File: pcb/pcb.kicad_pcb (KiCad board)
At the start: 2 copper layers, 201 x 76 mm, 21 parts, among them J1 encoder, J2 programmer, J4 usb-ttl, SW1 reset, SW2 play/pause, SW3 prev track, SW4 next track, U1 ATmega32-16P

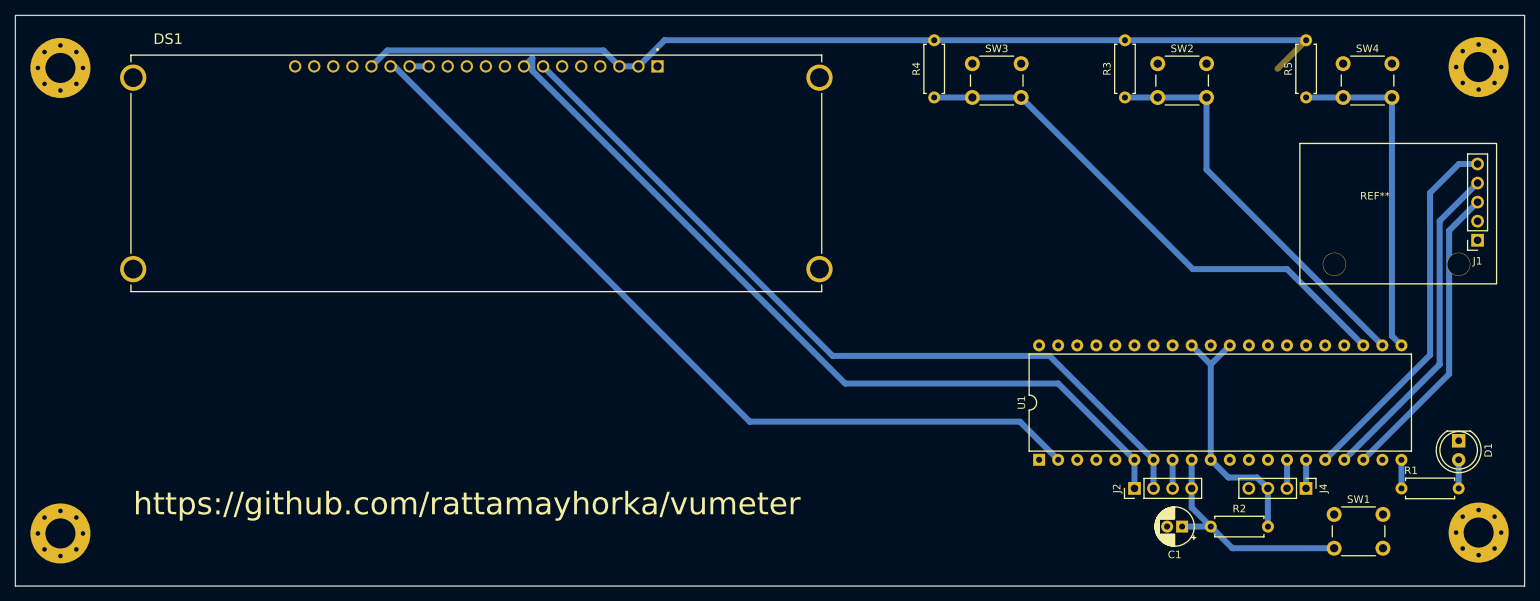
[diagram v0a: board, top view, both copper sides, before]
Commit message: add play/pause text
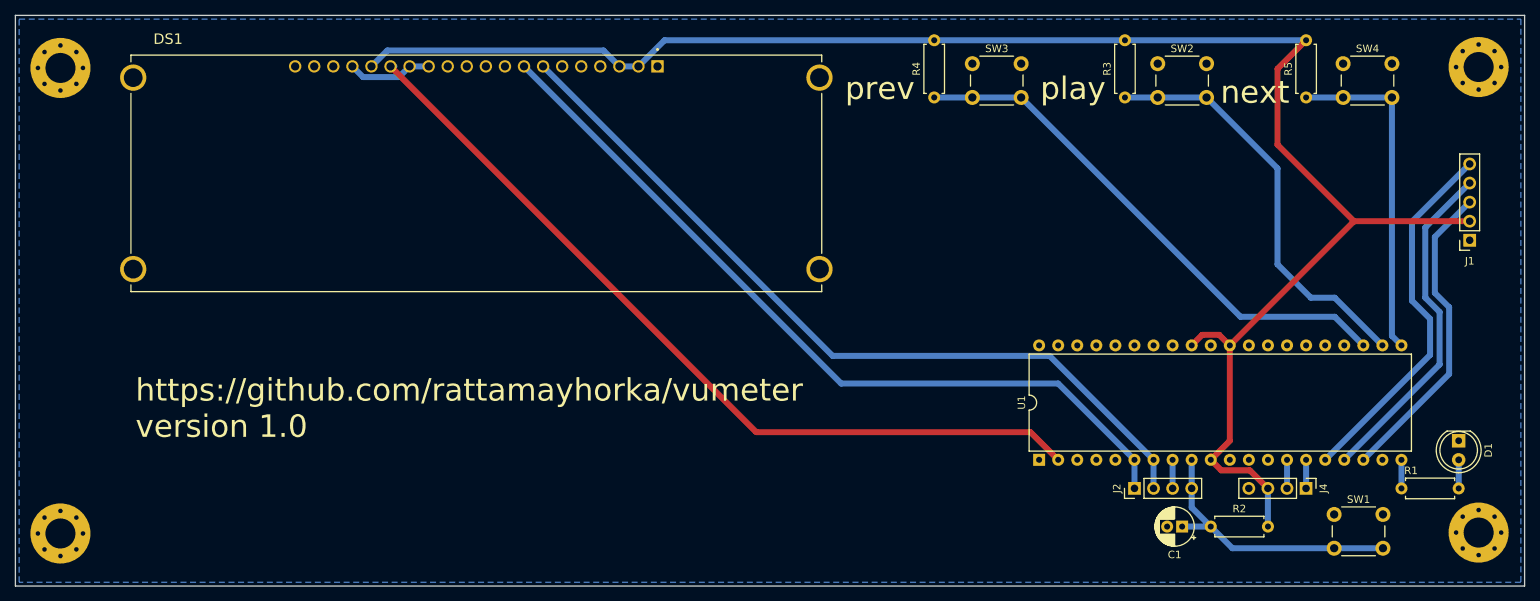
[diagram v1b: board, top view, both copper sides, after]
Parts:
- removed the REF** at (225.1, 89.1)
- moved J1 1.05 mm to (237.7, 94.0)
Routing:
- net +5V: track 167.2 -> 233.7 mm
- net GND: track 2.54 -> 11.3 mm
- net Net-(J2-Pin_4): track 31.4 -> 37.9 mm
- net Net-(DS1-DB1): track 108.7 -> 106.8 mm
- net Net-(U1-PC0): track 53.6 -> 55.5 mm
- net Net-(J1-Pin_4): track 44.2 -> 45.4 mm
- net Net-(J1-Pin_3): track 40.6 -> 41.8 mm
- net Net-(DS1-~{CS}): track 110.6 -> 111.1 mm
- added copper zone on B.Cu, net GND
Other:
- board text added: "https://github.com/rattamayhorka/vumeter version 1.0"
- board text added: "next"
- board text added: "play"
- board text added: "prev"
- board text removed: "https://github.com/rattamayhorka/vumeter"
